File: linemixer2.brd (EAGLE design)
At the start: 101.6 x 58.4 mm, 75 parts, among them IC1 OPA2134P, IC2 OPA2134P, IC3 OPA2134P, IC4 OPA2134P, IC5 OPA2134P, IC6 BUF634P, J1 POWER_JACK

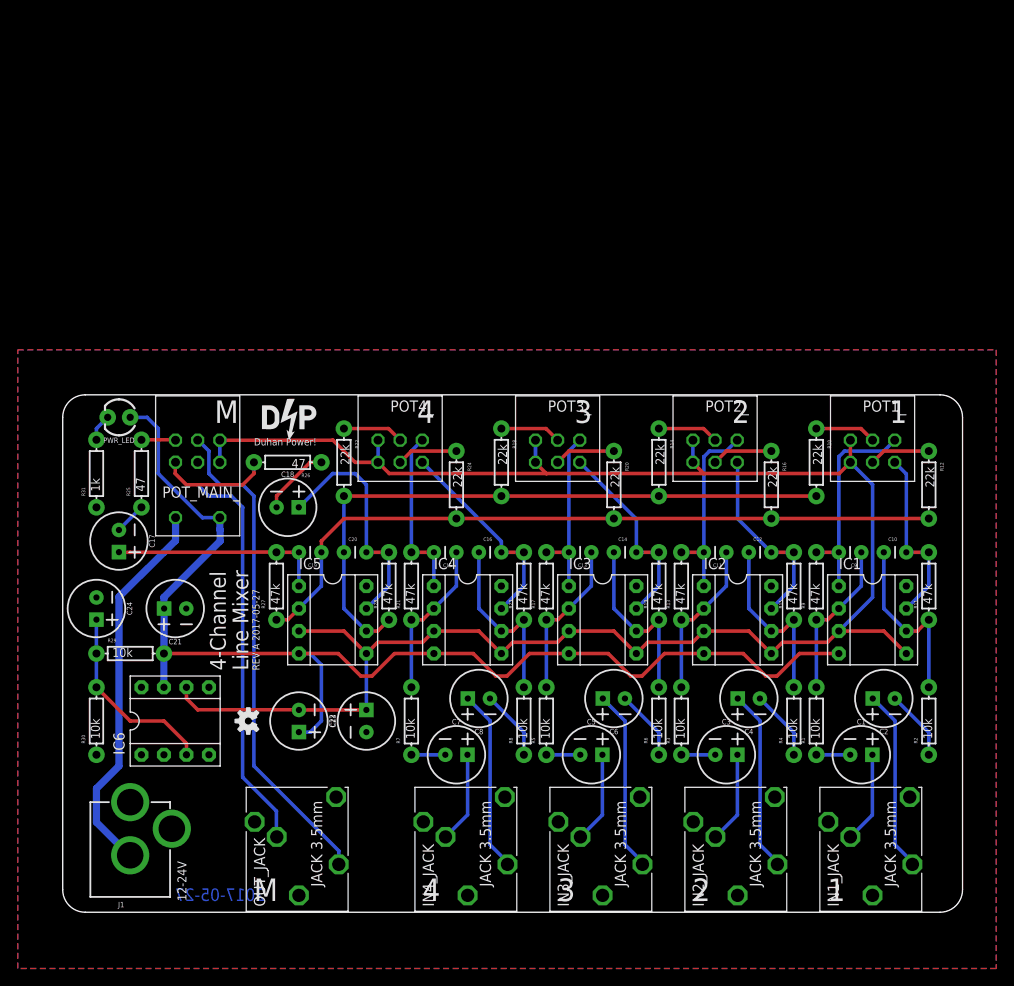
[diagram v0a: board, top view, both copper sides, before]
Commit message: change resistors to 3mm and tweak
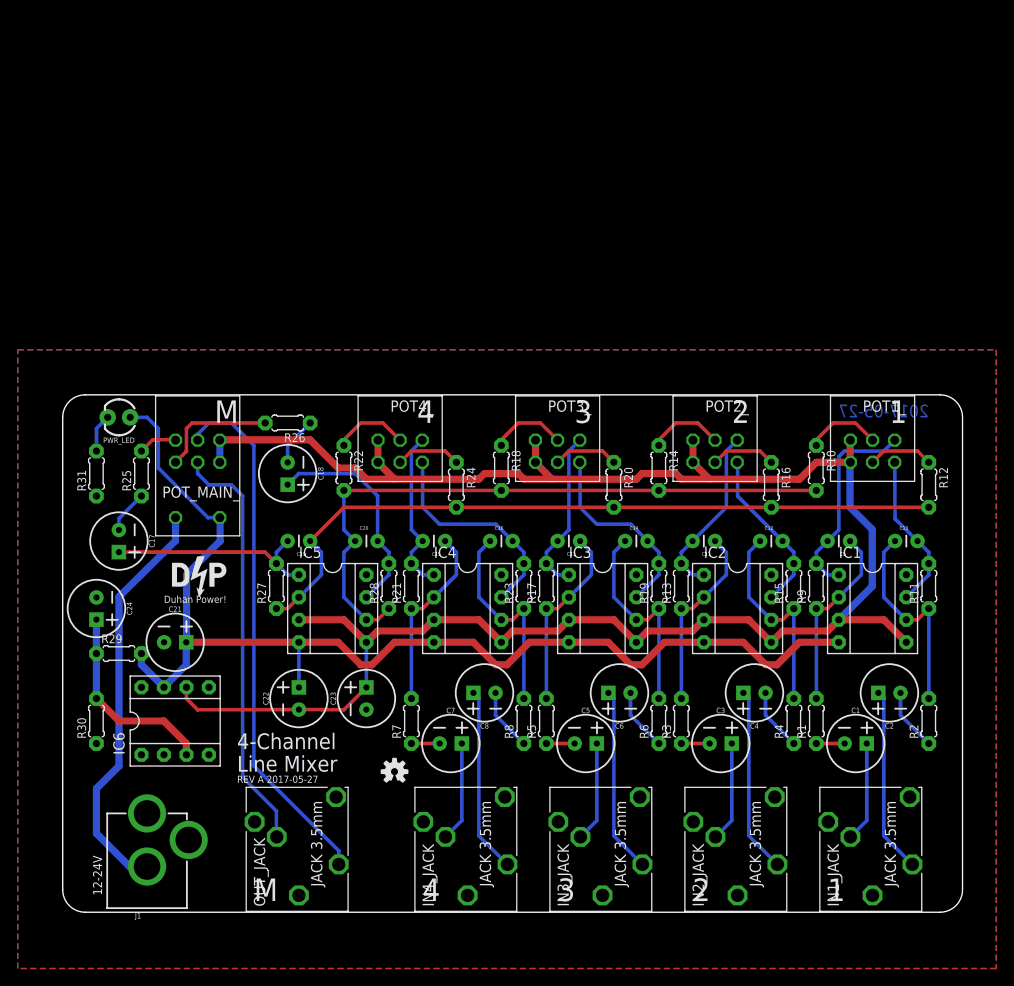
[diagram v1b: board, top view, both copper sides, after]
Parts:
- R1, R10, R11, R12, R13, R14, R15, R16, R17, R18, R19, R2, R20, R21, R22, R23, R24, R25, R26, R27, R28, R29, R3, R30, R31, R4, R5, R6, R7, R8, R9: device SparkFun-Resistors:AXIAL-0.3 -> adafruit:0204/5
- moved U$1 20.5 mm to (15.2, 38.1)
- moved LOGO1 17.5 mm to (37.5, 15.9), turned to 0 degrees
- moved R26 4.45 mm to (25.4, 55.2)
- moved C18 3.81 mm to (25.4, 49.5), turned to 270 degrees
- moved C21 3.81 mm to (12.7, 30.5), turned to 0 degrees
- moved C22 2.54 mm to (26.7, 24.1), turned to 90 degrees
- moved C23 2.54 mm to (34.3, 24.1)
- moved J1 2.29 mm to (9.53, -2.54)
- moved C10 1.80 mm to (94.0, 41.9)
- moved C11 1.80 mm to (73.7, 41.9)
- moved C14 1.80 mm to (63.5, 41.9)
- moved C15 1.80 mm to (43.2, 41.9)
- moved C20 1.80 mm to (33.0, 41.9)
- moved C19 1.80 mm to (27.9, 41.9)
- moved C12 1.80 mm to (78.7, 41.9)
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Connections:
- net BUS_L: now also R12.2, R16.2, R20.2, R24.2, R27.1; no longer R12.P$2, R16.P$2, R20.P$2, R24.P$2, R27.P$1
- net BUS_R: now also R10.2, R14.2, R18.2, R22.2, R28.1; no longer R10.P$2, R14.P$2, R18.P$2, R22.P$2, R28.P$1
- net GND: now also R30.1, R31.1; no longer R30.P$1, R31.P$1
- net IN1_L: now also R11.1, R2.2; no longer R11.P$1, R2.P$2
- net IN1_R: now also R1.2, R9.1; no longer R1.P$2, R9.P$1
- net IN2_L: now also R15.1, R4.2; no longer R15.P$1, R4.P$2
- net IN2_R: now also R13.1, R3.2; no longer R13.P$1, R3.P$2
- net IN3_L: now also R19.1, R6.2; no longer R19.P$1, R6.P$2
- net IN3_R: now also R17.1, R5.2; no longer R17.P$1, R5.P$2
- net IN4_L: now also R23.1, R8.2; no longer R23.P$1, R8.P$2
- net IN4_R: now also R21.1, R7.2; no longer R21.P$1, R7.P$2
- net N$10: now also R2.1; no longer R2.P$1
- net N$11: now also R3.1; no longer R3.P$1
- net N$12: now also R4.1; no longer R4.P$1
- net N$13: now also R5.1; no longer R5.P$1
- net N$14: now also R6.1; no longer R6.P$1
- net N$15: now also R7.1; no longer R7.P$1
- net N$16: now also R8.1; no longer R8.P$1
- net N$17: now also R9.2; no longer R9.P$2
- net N$18: now also R13.2; no longer R13.P$2
- net N$19: now also R10.1; no longer R10.P$1
- net N$20: now also R14.1; no longer R14.P$1
- net N$21: now also R11.2; no longer R11.P$2
- net N$22: now also R27.2; no longer R27.P$2
- net N$23: now also R28.2; no longer R28.P$2
- net N$24: now also R12.1; no longer R12.P$1
- net N$25: now also R15.2; no longer R15.P$2
- net N$26: now also R16.1; no longer R16.P$1
- net N$27: now also R17.2; no longer R17.P$2
- net N$28: now also R18.1; no longer R18.P$1
- net N$29: now also R19.2; no longer R19.P$2
- net N$30: now also R20.1; no longer R20.P$1
- net N$31: now also R21.2; no longer R21.P$2
- net N$32: now also R22.1; no longer R22.P$1
- net N$33: now also R23.2; no longer R23.P$2
- net N$34: now also R24.1; no longer R24.P$1
- net N$35: now also R25.1; no longer R25.P$1
- net N$36: now also R26.1; no longer R26.P$1
- net N$37: now also R25.2; no longer R25.P$2
- net N$38: now also R26.2; no longer R26.P$2
- net N$41: now also R31.2; no longer R31.P$2
- net N$44: now also R29.1, R30.2; no longer R29.P$1, R30.P$2
- net N$9: now also R1.1; no longer R1.P$1
- net VCC: now also R29.2; no longer R29.P$2
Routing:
- net VCC: track 136.7 -> 131.3 mm
- net VGND: track 217.6 -> 222.2 mm
- net OUT_R: track 56.0 -> 59.9 mm
- net N$42: track 43.5 -> 46.6 mm
- net IN2_R: track 18.1 -> 21.2 mm
- net IN4_R: track 18.1 -> 21.2 mm
- net IN1_R: track 18.1 -> 21.2 mm
- net IN3_R: track 18.1 -> 21.2 mm
- net IN3_L: track 20.6 -> 23.7 mm
- net IN1_L: track 20.6 -> 23.7 mm
- net IN4_L: track 20.6 -> 23.7 mm
- net IN2_L: track 20.6 -> 23.7 mm
- net N$21: track 20.6 -> 17.9 mm
- net N$25: track 21.7 -> 18.9 mm
- net N$23: track 27.3 -> 24.7 mm
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
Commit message: rev b
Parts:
- removed C24: 47u, SparkFun-Capacitors:CPOL-RADIAL-2.5MM-6.5MM
- removed IC6: BUF634P, burr-brown:DIL08
- removed R29, R30: 10k, adafruit:0204/5
- added U$2: TLE2426-TO_92, myparts:TO-92
- R1, R2, R3, R4, R5, R6, R7, R8: value 10k -> 1k
- R10, R12, R14, R16, R18, R20, R22, R24: value 22k -> 1k
- R11, R13, R15, R17, R19, R21, R23, R27, R28, R9: value 47k -> 1k
- R31: value 1k -> 5k
- moved C23 26.1 mm to (10.8, 35.6), turned to 270 degrees
- moved R31 21.9 mm to (25.4, 53.3), turned to 180 degrees
- moved U$1 14.3 mm to (28.6, 43.2)
- moved C22 13.3 mm to (14.0, 27.9), turned to 270 degrees
- moved C17 12.7 mm to (19.1, 41.9)
- moved PWR_LED 11.7 mm to (17.8, 53.3), turned to 0 degrees
- moved R26 11.2 mm to (17.8, 47.0)
- moved C21 10.3 mm to (10.8, 20.3), turned to 270 degrees
- moved R10 9.09 mm to (81.3, 41.9), turned to 90 degrees
- moved R22 9.09 mm to (35.6, 41.9), turned to 90 degrees
- moved R12 9.09 mm to (94.0, 40.0), turned to 90 degrees
- moved R24 9.09 mm to (48.3, 40.0), turned to 90 degrees
- moved R25 8.89 mm to (17.8, 49.5), turned to 180 degrees
- moved R14 8.35 mm to (66.0, 41.9), turned to 90 degrees
- moved R18 8.35 mm to (50.8, 41.9), turned to 90 degrees
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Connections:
- removed net N$19: POT1_.R1-W, R10.1
- removed net N$20: POT2_.R1-W, R14.1
- removed net N$24: POT1_.R2-W, R12.1
- removed net N$26: POT2_.R2-W, R16.1
- removed net N$28: POT3_.R1-W, R18.1
- removed net N$30: POT3_.R2-W, R20.1
- removed net N$32: POT4_.R1-W, R22.1
- removed net N$34: POT4_.R2-W, R24.1
- removed net N$44: C24.1, IC6.3, R29.1, R30.2
- new net N$40: C9.1, IC1.2, POT1_.R2-W, R9.1
- new net N$50: C13.1, IC3.2, POT3_.R2-W, R17.1
- new net N$51: C11.1, IC2.2, POT2_.R2-W, R13.1
- new net N$52: C15.1, IC4.2, POT4_.R2-W, R21.1
- new net N$60: C10.1, IC1.6, POT1_.R1-W, R11.1
- new net N$61: C12.1, IC2.6, POT2_.R1-W, R15.1
- new net N$62: C14.1, IC3.6, POT3_.R1-W, R19.1
- new net N$64: C16.1, IC4.6, POT4_.R1-W, R23.1
- net BUS_L: now also R10.2, R14.2, R18.2, R22.2; no longer R12.2, R16.2, R20.2, R24.2
- net BUS_R: now also R12.2, R16.2, R20.2, R24.2; no longer R10.2, R14.2, R18.2, R22.2
- net GND: now also POT1_.R1-A, POT1_.R2-A, POT2_.R1-A, POT2_.R2-A, POT3_.R1-A, POT3_.R2-A, POT4_.R1-A, POT4_.R2-A, POT_MAIN_.R1-A, POT_MAIN_.R2-A, U$2.PAD2; no longer C24.2, IC6.1, IC6.4, R30.1
- net IN1_L: now also POT1_.R2-B, R1.2; no longer C10.1, IC1.6, R11.1, R2.2
- net IN1_R: now also POT1_.R1-B, R2.2; no longer C9.1, IC1.2, R1.2, R9.1
- net IN2_L: now also POT2_.R2-B, R3.2; no longer C12.1, IC2.6, R15.1, R4.2
- net IN2_R: now also POT2_.R1-B, R4.2; no longer C11.1, IC2.2, R13.1, R3.2
- net IN3_L: now also POT3_.R2-B, R5.2; no longer C14.1, IC3.6, R19.1, R6.2
- net IN3_R: now also POT3_.R1-B, R6.2; no longer C13.1, IC3.2, R17.1, R5.2
- net IN4_L: now also POT4_.R2-B, R7.2; no longer C16.1, IC4.6, R23.1, R8.2
- net IN4_R: now also POT4_.R1-B, R8.2; no longer C15.1, IC4.2, R21.1, R7.2
- net N$17: now also R10.1; no longer POT1_.R1-B
- net N$18: now also R14.1; no longer POT2_.R1-B
- net N$21: now also R12.1; no longer POT1_.R2-B
- net N$25: now also R16.1; no longer POT2_.R2-B
- net N$27: now also R18.1; no longer POT3_.R1-B
- net N$29: now also R20.1; no longer POT3_.R2-B
- net N$31: now also R22.1; no longer POT4_.R1-B
- net N$33: now also R24.1; no longer POT4_.R2-B
- net OUT_L: now also POT_MAIN_.R1-W; no longer POT_MAIN_.R2-W
- net OUT_R: now also POT_MAIN_.R2-W; no longer POT_MAIN_.R1-W
- net VCC: now also U$2.PAD3; no longer IC6.7, R29.2
- net VGND: now also U$2.PAD1; no longer IC6.6, POT1_.R1-A, POT1_.R2-A, POT2_.R1-A, POT2_.R2-A, POT3_.R1-A, POT3_.R2-A, POT4_.R1-A, POT4_.R2-A, POT_MAIN_.R1-A, POT_MAIN_.R2-A
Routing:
- net VGND: track 222.2 -> 104.0 mm, vias 0 -> 1
- net N$64: track 0.00 -> 33.7 mm
- net N$62: track 0.00 -> 33.1 mm
- net N$61: track 0.00 -> 31.6 mm
- net N$60: track 0.00 -> 31.6 mm
- net N$44: track 22.4 -> 0.00 mm
- net N$52: track 0.00 -> 21.5 mm
- net N$40: track 0.00 -> 21.5 mm
- net N$50: track 0.00 -> 20.4 mm
- net N$51: track 0.00 -> 20.4 mm
- net VCC: track 131.3 -> 147.3 mm
- net N$33: track 24.8 -> 9.04 mm
- net N$17: track 23.3 -> 8.15 mm
- net N$22: track 24.4 -> 9.96 mm
- net BUS_L: track 82.4 -> 68.5 mm
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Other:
- board size 101.6 x 58.4 mm -> 96.5 x 55.9 mm
- board text added: "2017-06-12"
- board text added: "REV B 2017-06-12"
- board text removed: "2017-05-27"
- board text removed: "REV A 2017-05-27"

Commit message: rev B tweaks and images
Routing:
- net GND: track 0.00 -> 163.8 mm
- net VCC: track 147.3 -> 146.4 mm
- net N$42: track 42.5 -> 41.6 mm
- net VGND: vias 1 -> 0

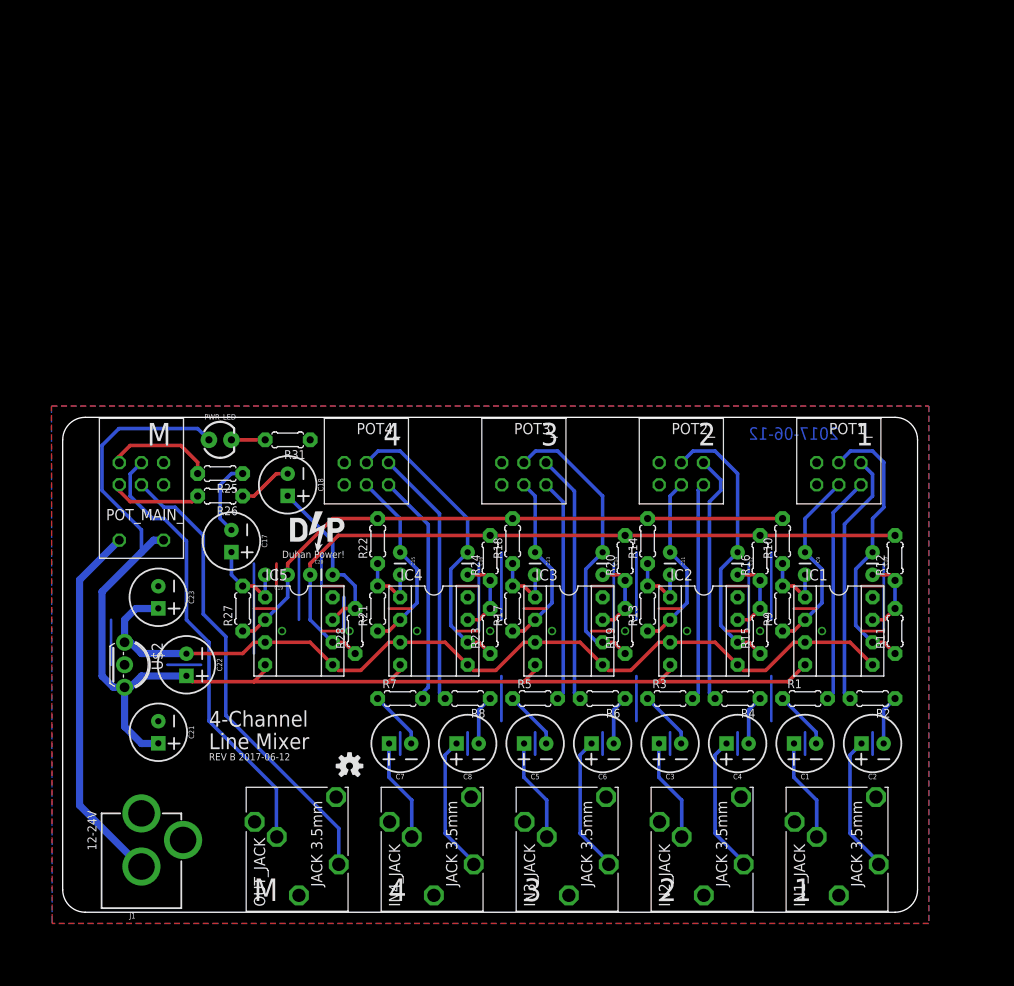
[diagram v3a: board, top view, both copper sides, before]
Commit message: rev c - add resistors to the vgnd on each opamp
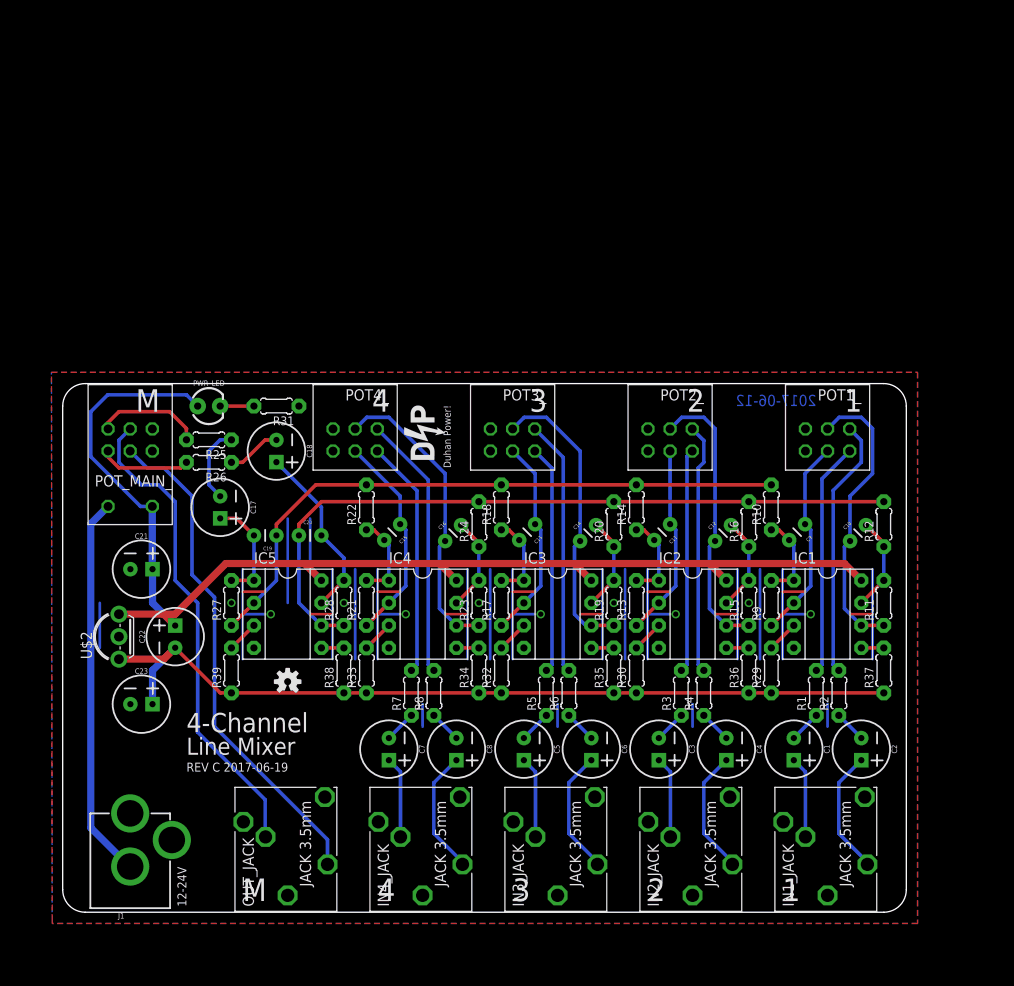
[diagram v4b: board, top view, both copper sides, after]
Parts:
- added R29, R30, R32, R33, R34, R35, R36, R37, R38, R39: 100k, adafruit:0204/5
- R31: value 5k -> 20k
- moved C21 18.5 mm to (8.89, 38.7), turned to 0 degrees
- moved U$1 16.2 mm to (40.6, 54.0), turned to 90 degrees
- moved C23 12.2 mm to (8.89, 23.5), turned to 0 degrees
- moved LOGO1 11.8 mm to (25.4, 26.0)
- moved C19 4.62 mm to (24.1, 42.5)
- moved C20 4.62 mm to (26.7, 42.5)
- moved R14 4.02 mm to (64.8, 45.7)
- moved POT3_ 4.02 mm to (50.8, 52.1)
- moved R22 4.02 mm to (34.3, 45.7)
- moved POT_MAIN_ 4.02 mm to (7.62, 52.1)
- moved C17 4.02 mm to (17.8, 45.7)
- moved C18 4.02 mm to (24.1, 52.1)
- moved R25 4.02 mm to (16.5, 53.3)
- moved POT1_ 4.02 mm to (86.4, 52.1)
- moved POT2_ 4.02 mm to (68.6, 52.1)
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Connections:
- new net N$19: IC1.3, R29.2
- new net N$20: IC5.3, R39.2
- new net N$24: IC5.5, R38.2
- new net N$30: IC2.3, R30.2
- new net N$34: IC3.3, R32.2
- new net N$44: IC4.3, R33.2
- new net N$46: IC4.5, R34.2
- new net N$48: IC3.5, R35.2
- new net N$53: IC2.5, R36.2
- new net N$55: IC1.5, R37.2
- net GND: now also IC1.4, IC2.4, IC3.4, IC4.4, IC5.4; no longer IC1.8, IC2.8, IC3.8, IC4.8, IC5.8
- net VCC: now also IC1.8, IC2.8, IC3.8, IC4.8, IC5.8; no longer IC1.4, IC2.4, IC3.4, IC4.4, IC5.4
- net VGND: now also R29.1, R30.1, R32.1, R33.1, R34.1, R35.1, R36.1, R37.1, R38.1, R39.1; no longer IC1.3, IC1.5, IC2.3, IC2.5, IC3.3, IC3.5, IC4.3, IC4.5, IC5.3, IC5.5
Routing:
- net GND: track 163.8 -> 210.8 mm, vias 9 -> 10
- net VGND: track 104.0 -> 96.4 mm
- net VCC: track 146.4 -> 141.8 mm
- net OUT_L: track 50.4 -> 54.6 mm
- net OUT_R: track 52.8 -> 57.0 mm
- net N$30: track 0.00 -> 3.59 mm
- net N$44: track 0.00 -> 3.59 mm
- net N$34: track 0.00 -> 3.59 mm
- net N$20: track 0.00 -> 3.59 mm
- net N$19: track 0.00 -> 3.59 mm
- net N$13: track 6.65 -> 3.61 mm
- net N$15: track 6.65 -> 3.61 mm
- net N$11: track 6.65 -> 3.61 mm
- net N$9: track 6.65 -> 3.61 mm
- net BUS_L: track 68.5 -> 71.3 mm
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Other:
- board size 96.5 x 55.9 mm -> 95.2 x 59.7 mm
- board text added: "REV C 2017-06-19"
- board text removed: "REV B 2017-06-12"

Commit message: rev D
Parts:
- added U$3: DP_LOGO, myparts:DP_LOGO
- moved LOGO1 73.5 mm to (96.0, 5.40), turned to 90 degrees
- moved U$1 3.51 mm to (43.0, 51.4), turned to 0 degrees
- moved C18 2.84 mm to (25.4, 49.5), turned to 0 degrees
- moved PWR_LED 2.60 mm to (18.8, 55.9)
- moved R25 2.29 mm to (18.4, 52.1)
- moved R26 2.29 mm to (18.4, 49.5)
- moved C17 1.80 mm to (19.1, 44.5), turned to 0 degrees
- moved R31 1.62 mm to (25.1, 55.9)
- moved C19 1.18 mm to (25.1, 41.9)
- moved C20 1.18 mm to (27.7, 41.9)
- moved J1 1.12 mm to (8.62, -3.04)
- moved C1 1.00 mm to (83.5, 18.4)
- moved C10 1.00 mm to (89.9, 41.9)
- moved C11 1.00 mm to (69.6, 43.8)
- moved C12 1.00 mm to (74.7, 41.9)
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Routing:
- net GND: track 210.8 -> 205.7 mm
- net N$36: track 6.12 -> 3.20 mm
- net G4: track 0.00 -> 2.00 mm
- net G3: track 0.00 -> 2.00 mm
- net N$23: track 20.1 -> 18.1 mm
- net N$22: track 12.2 -> 10.5 mm
- net N$37: track 12.2 -> 13.8 mm
- net N$41: track 3.81 -> 2.54 mm
- net N$38: track 10.3 -> 11.2 mm
- net N$42: track 43.4 -> 43.9 mm
- added copper zone on layer 1, net G3
- added copper zone on layer 1, net G4
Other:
- board size 95.2 x 59.7 mm -> 98.3 x 100 mm
- board text added: "2017-06-19"
- board text added: "DC IN 12-24V"
- board text added: "LINE"
- board text added: "MIXER"
- board text added: "REV D 2017-06-19"
- board text added: "https://github.com/andrewduhan/linemixer2"
- board text removed: "2017-06-12"
- board text removed: "M"
- board text removed: "REV C 2017-06-19"
